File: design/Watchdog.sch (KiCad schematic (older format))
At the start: 25 parts, among them U401 STWD100xxWY, U402 STWD100xxWY, U403 74LVC2G00, U405 74AHC157, U406 74LV14

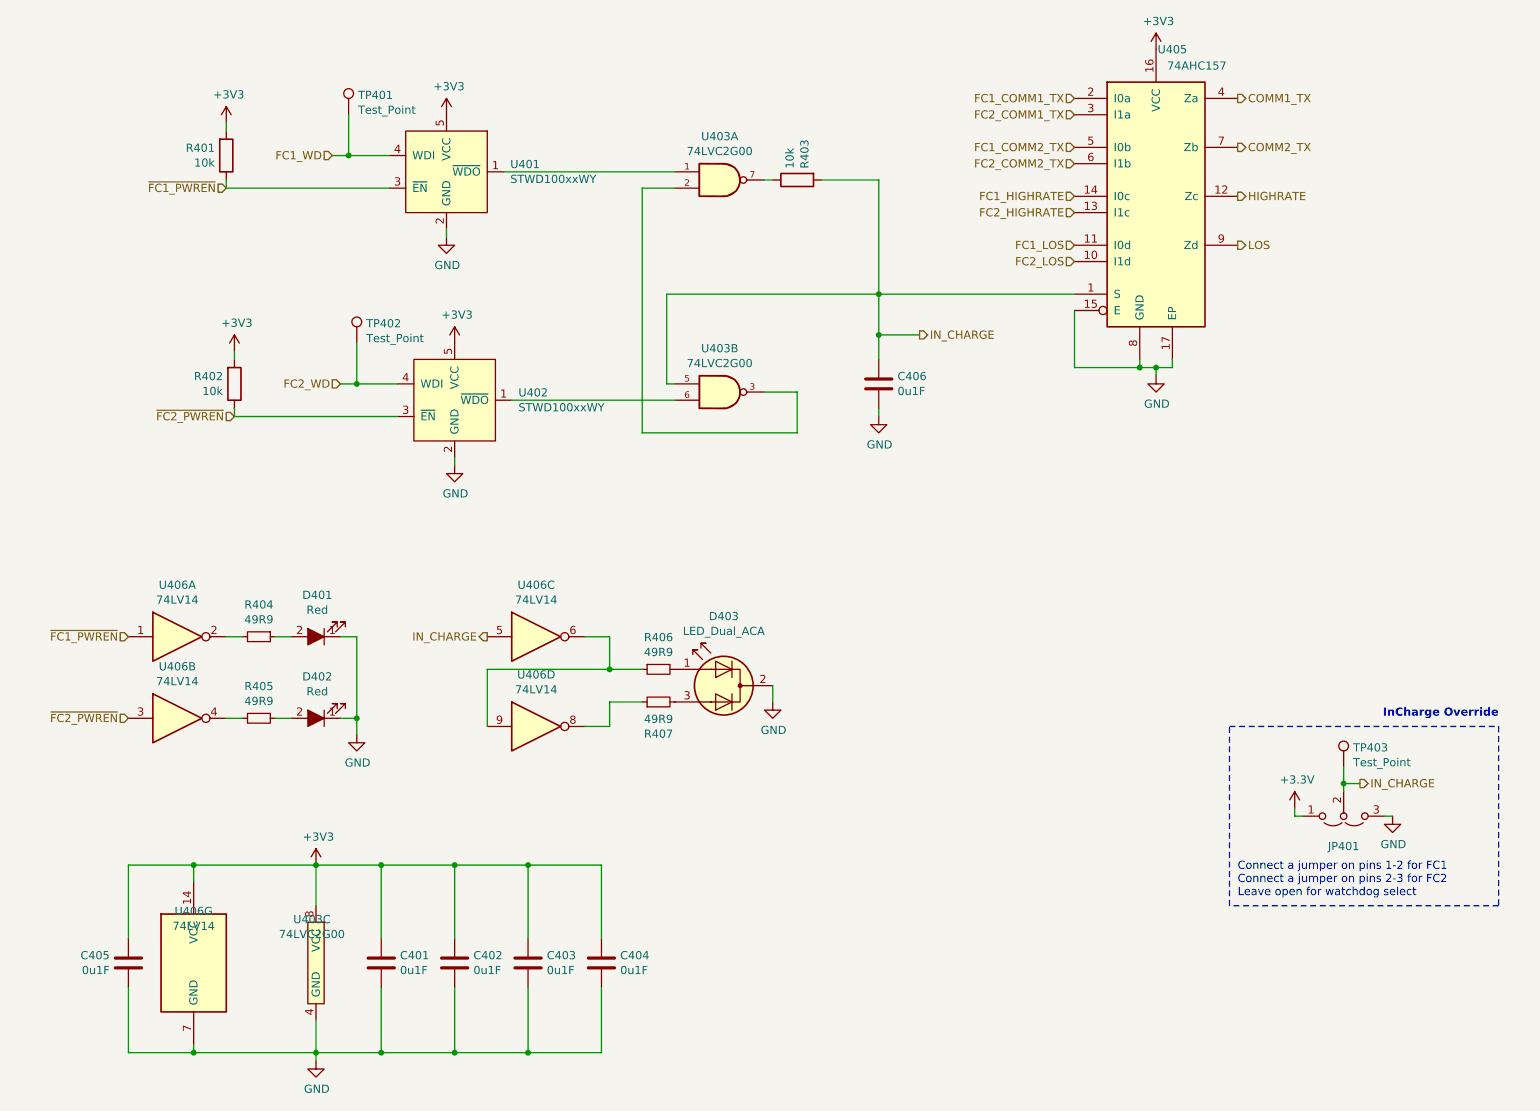
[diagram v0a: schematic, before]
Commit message: Renumber and sub clock generator
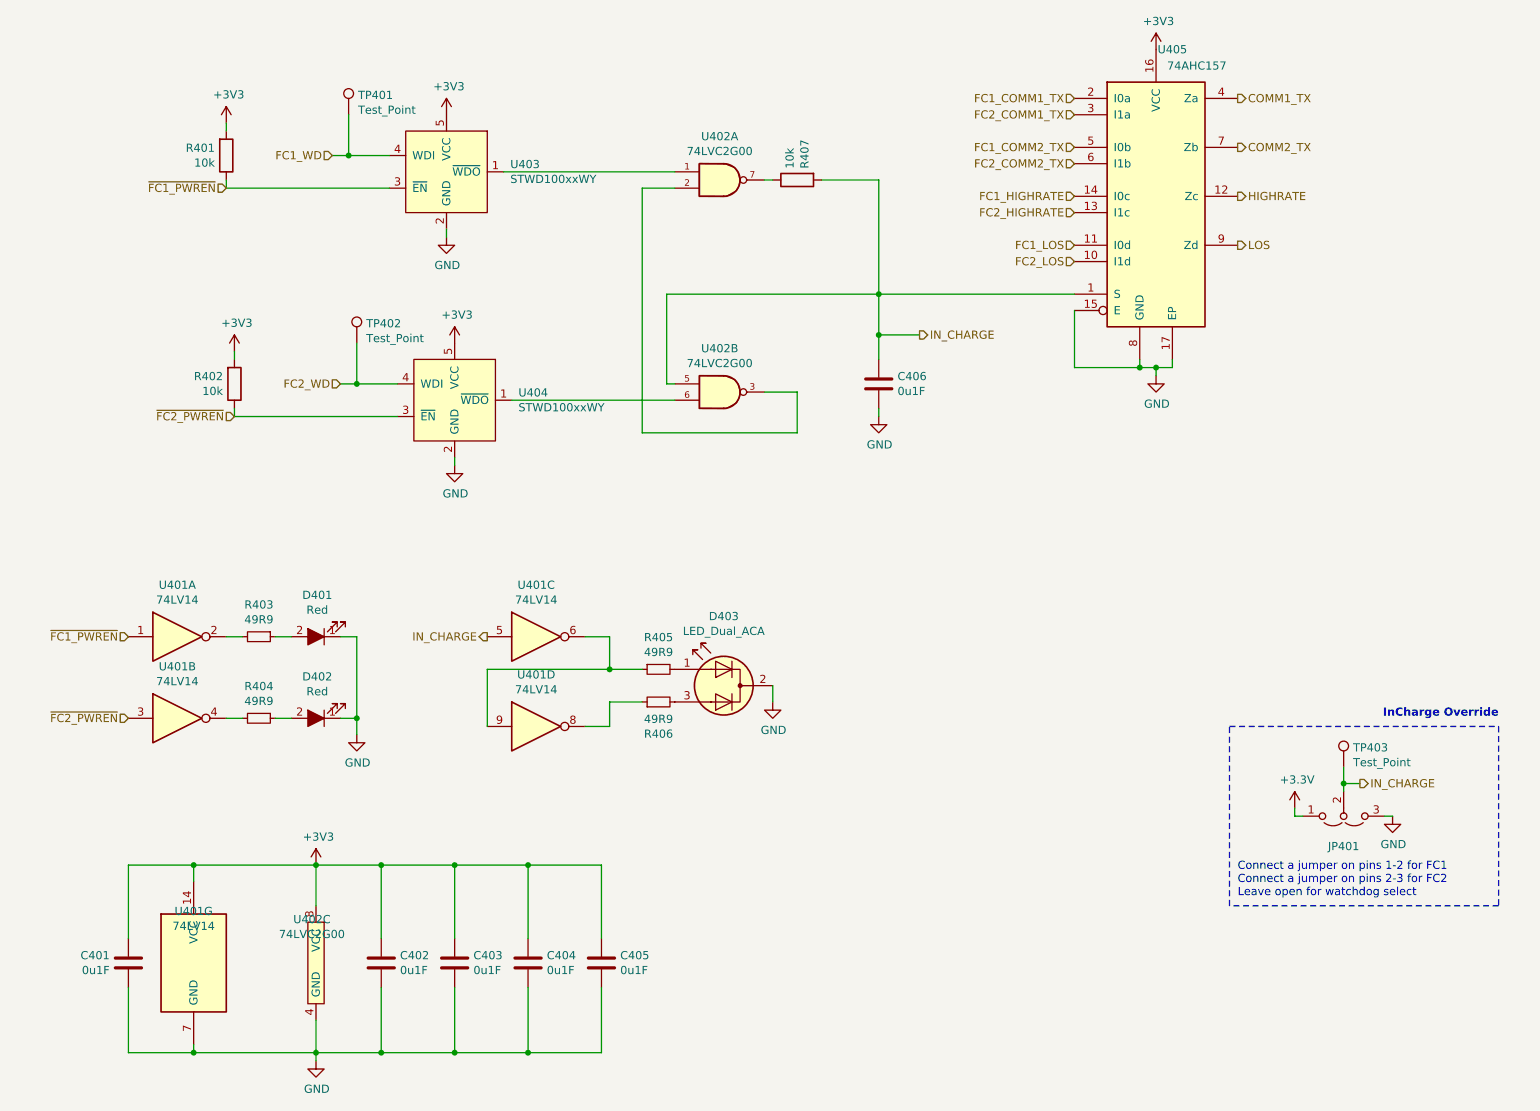
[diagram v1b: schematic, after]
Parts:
- renumbered C405 to C401, C401 to C402, C402 to C403, C403 to C404, C404 to C405, R404 to R403, R405 to R404, R406 to R405, R407 to R406, R403 to R407, U406 to U401, U403 to U402, U401 to U403, U402 to U404
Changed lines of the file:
@@
 $EndDescr
 $Comp
-L CommsCard:STWD100xxWY U402
+L CommsCard:STWD100xxWY U404
 U 1 1 5A7B0FE8
 P 4450 3250
-F 0 "U402" H 4841 3296 50  0000 L CNN
+F 0 "U404" H 4841 3296 50  0000 L CNN
 F 1 "STWD100xxWY" H 4841 3205 50  0000 L CNN
 F 2 "Package_TO_SOT_SMD:SOT-353_SC-70-5" H 4500 3450 50  0001 C CNN
@@
 $EndComp
 $Comp
-L CommsCard:74LVC2G00 U403
+L CommsCard:74LVC2G00 U402
 U 2 1 5A7B6676
 P 6100 3200
-F 0 "U403" H 6075 3467 50  0000 C CNN
+F 0 "U402" H 6075 3467 50  0000 C CNN
 F 1 "74LVC2G00" H 6075 3376 50  0000 C CNN
 F 2 "Package_SO:VSSOP-8_2.3x2mm_P0.5mm" H 6100 3200 50  0001 C CNN
@@
 	5800 1850 4750 1850
 $Comp
-L power:GND #PWR0404
+L power:GND #PWR0407
 U 1 1 5A7B7021
 P 4400 2250
-F 0 "#PWR0404" H 4400 2000 50  0001 C CNN
+F 0 "#PWR0407" H 4400 2000 50  0001 C CNN
 F 1 "GND" H 4405 2077 50  0000 C CNN
 F 2 "" H 4400 2250 50  0001 C CNN
@@
 	4400 2250 4400 2200
 $Comp
-L power:GND #PWR0406
+L power:GND #PWR0409
 U 1 1 5A7B7145
 P 4450 3650
-F 0 "#PWR0406" H 4450 3400 50  0001 C CNN
+F 0 "#PWR0409" H 4450 3400 50  0001 C CNN
 F 1 "GND" H 4455 3477 50  0000 C CNN
 F 2 "" H 4450 3650 50  0001 C CNN
@@
 	4450 3650 4450 3600
 $Comp
-L CommsCard:74LVC2G00 U403
+L CommsCard:74LVC2G00 U402
 U 1 1 5A7B74F5
 P 6100 1900
-F 0 "U403" H 6075 2167 50  0000 C CNN
+F 0 "U402" H 6075 2167 50  0000 C CNN
 F 1 "74LVC2G00" H 6075 2076 50  0000 C CNN
 F 2 "Package_SO:VSSOP-8_2.3x2mm_P0.5mm" H 6100 1900 50  0001 C CNN
@@
 ~FC1_PWREN
 $Comp
-L power:+3V3 #PWR0405
+L power:+3V3 #PWR0408
 U 1 1 5A7B9113
 P 4450 2900
-F 0 "#PWR0405" H 4450 2750 50  0001 C CNN
+F 0 "#PWR0408" H 4450 2750 50  0001 C CNN
 F 1 "+3V3" H 4465 3073 50  0000 C CNN
 F 2 "" H 4450 2900 50  0001 C CNN
@@
 $EndComp
 $Comp
-L power:+3V3 #PWR0403
+L power:+3V3 #PWR0406
 U 1 1 5A7B9130
 P 4400 1500
-F 0 "#PWR0403" H 4400 1350 50  0001 C CNN
+F 0 "#PWR0406" H 4400 1350 50  0001 C CNN
 F 1 "+3V3" H 4415 1673 50  0000 C CNN
 F 2 "" H 4400 1500 50  0001 C CNN
@@
 Connection ~ 7050 2600
 $Comp
-L power:+3V3 #PWR0409
+L power:+3V3 #PWR0412
 U 1 1 5A7BE16C
 P 8750 1100
-F 0 "#PWR0409" H 8750 950 50  0001 C CNN
+F 0 "#PWR0412" H 8750 950 50  0001 C CNN
 F 1 "+3V3" H 8765 1273 50  0000 C CNN
 F 2 "" H 8750 1100 50  0001 C CNN
@@
 $EndComp
 $Comp
-L power:GND #PWR0410
+L power:GND #PWR0413
 U 1 1 5A7BE18B
 P 8750 3100
-F 0 "#PWR0410" H 8750 2850 50  0001 C CNN
+F 0 "#PWR0413" H 8750 2850 50  0001 C CNN
 F 1 "GND" H 8755 2927 50  0000 C CNN
 F 2 "" H 8750 3100 50  0001 C CNN
@@
 Connection ~ 8750 3050
 $Comp
-L CommsCard:74LVC2G00 U403
+L CommsCard:74LVC2G00 U402
 U 3 1 5A7BD6BD
 P 3600 6700
-F 0 "U403" H 3575 6967 50  0000 C CNN
+F 0 "U402" H 3575 6967 50  0000 C CNN
 F 1 "74LVC2G00" H 3575 6876 50  0000 C CNN
 F 2 "Package_SO:VSSOP-8_2.3x2mm_P0.5mm" H 3600 6700 50  0001 C CNN
@@
 $EndComp
 $Comp
-L power:+3V3 #PWR0407
+L power:+3V3 #PWR0403
 U 1 1 5A7BD74A
 P 3600 6100
-F 0 "#PWR0407" H 3600 5950 50  0001 C CNN
+F 0 "#PWR0403" H 3600 5950 50  0001 C CNN
 F 1 "+3V3" H 3615 6273 50  0000 C CNN
 F 2 "" H 3600 6100 50  0001 C CNN
@@
 $EndComp
 $Comp
-L power:GND #PWR0408
+L power:GND #PWR0404
 U 1 1 5A7BD781
 P 3600 7300
-F 0 "#PWR0408" H 3600 7050 50  0001 C CNN
+F 0 "#PWR0404" H 3600 7050 50  0001 C CNN
 F 1 "GND" H 3605 7127 50  0000 C CNN
 F 2 "" H 3600 7300 50  0001 C CNN
@@
 $EndComp
 $Comp
-L CommsCard:STWD100xxWY U401
+L CommsCard:STWD100xxWY U403
 U 1 1 5A7BE12B
 P 4400 1850
-F 0 "U401" H 4791 1896 50  0000 L CNN
+F 0 "U403" H 4791 1896 50  0000 L CNN
 F 1 "STWD100xxWY" H 4791 1805 50  0000 L CNN
 F 2 "Package_TO_SOT_SMD:SOT-353_SC-70-5" H 4450 2050 50  0001 C CNN
@@
 	4000 6850 4000 7250
 $Comp
-L Device:C C401
+L Device:C C402
 U 1 1 5A7C0E16
 P 4000 6700
-F 0 "C401" H 4115 6746 50  0000 L CNN
+F 0 "C402" H 4115 6746 50  0000 L CNN
 F 1 "0u1F" H 4115 6655 50  0000 L CNN
 F 2 "Capacitor_SMD:C_0603_1608Metric" H 4038 6550 50  0001 C CNN
@@
 	4450 6850 4450 7250
 $Comp
-L Device:C C402
+L Device:C C403
 U 1 1 5A7C13BB
 P 4450 6700
-F 0 "C402" H 4565 6746 50  0000 L CNN
+F 0 "C403" H 4565 6746 50  0000 L CNN
 F 1 "0u1F" H 4565 6655 50  0000 L CNN
 F 2 "Capacitor_SMD:C_0603_1608Metric" H 4488 6550 50  0001 C CNN
@@
 	4900 6850 4900 7250
 $Comp
-L Device:C C403
+L Device:C C404
 U 1 1 5A7C1A22
 P 4900 6700
-F 0 "C403" H 5015 6746 50  0000 L CNN
+F 0 "C404" H 5015 6746 50  0000 L CNN
 F 1 "0u1F" H 5015 6655 50  0000 L CNN
 F 2 "Capacitor_SMD:C_0603_1608Metric" H 4938 6550 50  0001 C CNN
@@
 	5350 6850 5350 7250
 $Comp
-L Device:C C404
+L Device:C C405
 U 1 1 5A7C1A2B
 P 5350 6700
-F 0 "C404" H 5465 6746 50  0000 L CNN
+F 0 "C405" H 5465 6746 50  0000 L CNN
 F 1 "0u1F" H 5465 6655 50  0000 L CNN
 F 2 "Capacitor_SMD:C_0603_1608Metric" H 5388 6550 50  0001 C CNN
@@
 $EndComp
 $Comp
-L Device:R R403
+L Device:R R407
 U 1 1 5A836CA1
 P 6550 1900
-F 0 "R403" H 6480 1854 50  0000 R CNN
+F 0 "R407" H 6480 1854 50  0000 R CNN
 F 1 "10k" H 6480 1945 50  0000 R CNN
 F 2 "Resistor_SMD:R_0603_1608Metric" V 6480 1900 50  0001 C CNN
@@
 $EndComp
 $Comp
-L Device:R_Small R404
+L Device:R_Small R403
 U 1 1 5A83AF0C
 P 3250 4700
-F 0 "R404" V 3054 4700 50  0000 C CNN
+F 0 "R403" V 3054 4700 50  0000 C CNN
 F 1 "49R9" V 3145 4700 50  0000 C CNN
 F 2 "Resistor_SMD:R_0603_1608Metric" H 3250 4700 50  0001 C CNN
@@
 ~FC1_PWREN
 $Comp
-L power:GND #PWR0411
+L power:GND #PWR0405
 U 1 1 5A83E020
 P 3850 5300
-F 0 "#PWR0411" H 3850 5050 50  0001 C CNN
+F 0 "#PWR0405" H 3850 5050 50  0001 C CNN
 F 1 "GND" H 3855 5127 50  0000 C CNN
 F 2 "" H 3850 5300 50  0001 C CNN
@@
 	3350 5200 3450 5200
 $Comp
-L Logic_74xx:74HC04 U406
+L Logic_74xx:74HC04 U401
 U 3 1 5A8462FD
 P 4950 4700
-F 0 "U406" H 4950 5017 50  0000 C CNN
+F 0 "U401" H 4950 5017 50  0000 C CNN
 F 1 "74LV14" H 4950 4926 50  0000 C CNN
 F 2 "Package_SO:TSSOP-14_4.4x5mm_P0.65mm" H 4950 4700 50  0001 C CNN
@@
 $EndComp
 $Comp
-L Device:R_Small R405
+L Device:R_Small R404
 U 1 1 5A84653F
 P 3250 5200
-F 0 "R405" V 3054 5200 50  0000 C CNN
+F 0 "R404" V 3054 5200 50  0000 C CNN
 F 1 "49R9" V 3145 5200 50  0000 C CNN
 F 2 "Resistor_SMD:R_0603_1608Metric" H 3250 5200 50  0001 C CNN
@@
 $EndComp
 $Comp
-L Device:R_Small R406
+L Device:R_Small R405
 U 1 1 5A846591
 P 5700 4900
-F 0 "R406" V 5504 4900 50  0000 C CNN
+F 0 "R405" V 5504 4900 50  0000 C CNN
 F 1 "49R9" V 5595 4900 50  0000 C CNN
 F 2 "Resistor_SMD:R_0603_1608Metric" H 5700 4900 50  0001 C CNN
@@
 	5400 4900 5400 4700
 $Comp
-L Device:R_Small R407
+L Device:R_Small R406
 U 1 1 5A84C00E
 P 5700 5100
-F 0 "R407" V 5504 5100 50  0000 C CNN
+F 0 "R406" V 5504 5100 50  0000 C CNN
 F 1 "49R9" V 5595 5100 50  0000 C CNN
 F 2 "Resistor_SMD:R_0603_1608Metric" H 5700 5100 50  0001 C CNN
@@
 IN_CHARGE
 $Comp
-L power:GND #PWR0412
+L power:GND #PWR0410
 U 1 1 5A8484FB
 P 6400 5100
-F 0 "#PWR0412" H 6400 4850 50  0001 C CNN
+F 0 "#PWR0410" H 6400 4850 50  0001 C CNN
 F 1 "GND" H 6405 4927 50  0000 C CNN
 F 2 "" H 6400 5100 50  0001 C CNN
@@
 	2450 6850 2450 7250
 $Comp
-L Device:C C405
+L Device:C C401
 U 1 1 5A84E9D4
 P 2450 6700
-F 0 "C405" H 2565 6746 50  0000 L CNN
+F 0 "C401" H 2565 6746 50  0000 L CNN
 F 1 "0u1F" H 2565 6655 50  0000 L CNN
 F 2 "Capacitor_SMD:C_0603_1608Metric" H 2488 6550 50  0001 C CNN
@@
 	2850 7250 2450 7250
 $Comp
-L Logic_74xx:74HC04 U406
+L Logic_74xx:74HC04 U401
 U 4 1 5A85B128
 P 4950 5250
-F 0 "U406" H 4950 5567 50  0000 C CNN
+F 0 "U401" H 4950 5567 50  0000 C CNN
 F 1 "74LV14" H 4950 5476 50  0000 C CNN
 F 2 "Package_SO:TSSOP-14_4.4x5mm_P0.65mm" H 4950 5250 50  0001 C CNN
@@
 $EndComp
 $Comp
-L Logic_74xx:74HC04 U406
+L Logic_74xx:74HC04 U401
 U 2 1 5A85B182
 P 2750 5200
-F 0 "U406" H 2750 5517 50  0000 C CNN
+F 0 "U401" H 2750 5517 50  0000 C CNN
 F 1 "74LV14" H 2750 5426 50  0000 C CNN
 F 2 "Package_SO:TSSOP-14_4.4x5mm_P0.65mm" H 2750 5200 50  0001 C CNN
@@
 $EndComp
 $Comp
-L Logic_74xx:74HC04 U406
+L Logic_74xx:74HC04 U401
 U 1 1 5A85B1F6
 P 2750 4700
-F 0 "U406" H 2750 5017 50  0000 C CNN
+F 0 "U401" H 2750 5017 50  0000 C CNN
 F 1 "74LV14" H 2750 4926 50  0000 C CNN
 F 2 "Package_SO:TSSOP-14_4.4x5mm_P0.65mm" H 2750 4700 50  0001 C CNN
@@
 $EndComp
 $Comp
-L Logic_74xx:74HC04 U406
+L Logic_74xx:74HC04 U401
 U 7 1 5A85B26F
 P 2850 6700
-F 0 "U406" H 2850 7017 50  0000 C CNN
+F 0 "U401" H 2850 7017 50  0000 C CNN
 F 1 "74LV14" H 2850 6926 50  0000 C CNN
 F 2 "Package_SO:TSSOP-14_4.4x5mm_P0.65mm" H 2850 6700 50  0001 C CNN
@@
 $EndComp
 $Comp
-L power:GND #PWR0414
+L power:GND #PWR0415
 U 1 1 5A86F4D1
 P 10200 5800
-F 0 "#PWR0414" H 10200 5550 50  0001 C CNN
+F 0 "#PWR0415" H 10200 5550 50  0001 C CNN
 F 1 "GND" H 10205 5627 50  0000 C CNN
 F 2 "" H 10200 5800 50  0001 C CNN
@@
 $EndComp
 $Comp
-L power:+3.3V #PWR0413
+L power:+3.3V #PWR0414
 U 1 1 5A86F4DF
 P 9600 5750
-F 0 "#PWR0413" H 9600 5600 50  0001 C CNN
+F 0 "#PWR0414" H 9600 5600 50  0001 C CNN
 F 1 "+3.3V" H 9615 5923 50  0000 C CNN
 F 2 "" H 9600 5750 50  0001 C CNN
@@
 $EndComp
 $Comp
-L power:GND #PWR0415
+L power:GND #PWR0411
 U 1 1 5A88736C
 P 7050 3350
-F 0 "#PWR0415" H 7050 3100 50  0001 C CNN
+F 0 "#PWR0411" H 7050 3100 50  0001 C CNN
 F 1 "GND" H 7055 3177 50  0000 C CNN
 F 2 "" H 7050 3350 50  0001 C CNN
